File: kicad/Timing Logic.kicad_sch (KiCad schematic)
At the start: 38 parts, among them Q2 BC108, Q3 BC108, Q4 BD139, Q5 BC108, Q6 BC108, SW6 SW_SPDT, U6 4043, U7 4017, U8 HEF4093B, U9 TL431LP

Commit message: Starting docs
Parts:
- D14: footprint Diode_THT:D_DO-41_SOD81_P12.70mm_Horizontal -> Diode_THT:D_DO-35_SOD27_P7.62mm_Horizontal
- U9: footprint Package_TO_SOT_THT:TO-92 -> Package_TO_SOT_THT:TO-92_Inline
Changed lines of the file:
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@@
 (kicad_sch
-	(version 20231120)
+	(version 20250114)
 	(generator "eeschema")
-	(generator_version "8.0")
+	(generator_version "9.0")
 	(paper "A3")
 	(title_block
 		(title "PROM Programmer")
-		(date "2024-11-17")
-		(rev "V1.1")
+		(date "2025-03-27")
+		(rev "V1.4")
+	)
+	(text "Program\n(Push Button)\n"
+		(exclude_from_sim no)
+		(at 201.93 120.396 0)
+		(effects
+			(font
+				(size 1.27 1.27)
+			)
+		)
+	)
+	(text "Program"
+		(exclude_from_sim no)
+		(at 291.084 183.388 0)
+		(effects
+			(font
+				(size 1.27 1.27)
+			)
+		)
+	)
+	(text "Constant Current Source (65mA)\n"
+		(exclude_from_sim no)
+		(at 215.138 35.56 0)
+		(effects
+			(font
+				(size 1.27 1.27)
+			)
+		)
+	)
+	(text "Resistor = 2.5 / Io \nR = 16/0.065 = 38 \n\nIo = 2.5/47 = 53mA\n\nR = 1/(1/47 + 1/220) = 38.2\n"
+		(exclude_from_sim no)
+		(at 255.778 56.896 0)
+		(effects
+			(font
+				(size 1.27 1.27)
+			)
+		)
+	)
+	(text "Optional R to give \nvery close value\n"
+		(exclude_from_sim no)
+		(at 246.38 68.58 0)
+		(effects
+			(font
+				(size 0.635 0.635)
+			)
+		)
+	)
+	(text "0 = 10V Ouput\n1 = 0V output (BD139 shut down)"
+		(exclude_from_sim no)
+		(at 335.534 151.13 0)
+		(effects
+			(font
+				(size 1.27 1.27)
+			)
+			(justify left)
+		)
 	)
 	(junction
@@
 		)
 	)
-	(text "Program\n(Push Button)\n"
-		(exclude_from_sim no)
-		(at 201.93 120.396 0)
-		(effects
-			(font
-				(size 1.27 1.27)
-			)
-		)
-	)
-	(text "Program"
-		(exclude_from_sim no)
-		(at 291.084 183.388 0)
-		(effects
-			(font
-				(size 1.27 1.27)
-			)
-		)
-	)
-	(text "Constant Current Source (65mA)\n"
-		(exclude_from_sim no)
-		(at 215.138 35.56 0)
-		(effects
-			(font
-				(size 1.27 1.27)
-			)
-		)
-	)
-	(text "Resistor = 2.5 / Io \nR = 16/0.065 = 38 \n\nIo = 2.5/47 = 53mA\n\nR = 1/(1/47 + 1/220) = 38.2\n"
-		(exclude_from_sim no)
-		(at 255.778 56.896 0)
-		(effects
-			(font
-				(size 1.27 1.27)
-			)
-		)
-	)
-	(text "Optional R to give \nvery close value\n"
-		(exclude_from_sim no)
-		(at 246.38 68.58 0)
-		(effects
-			(font
-				(size 0.635 0.635)
-			)
-		)
-	)
-	(text "0 = 10V Ouput\n1 = 0V output (BD139 shut down)"
-		(exclude_from_sim no)
-		(at 335.534 151.13 0)
-		(effects
-			(font
-				(size 1.27 1.27)
-			)
-			(justify left)
-		)
-	)
 	(global_label "START"
 		(shape output)
@@
 			)
 		)
-		(property "Footprint" "Package_TO_SOT_THT:TO-92"
+		(property "Footprint" "Package_TO_SOT_THT:TO-92_Inline"
 			(at 207.264 63.5 0)
 			(effects
@@
 			)
 		)
-		(property "Footprint" "Diode_THT:D_DO-41_SOD81_P12.70mm_Horizontal"
+		(property "Footprint" "Diode_THT:D_DO-35_SOD27_P7.62mm_Horizontal"
 			(at 330.2 143.51 0)
 			(effects

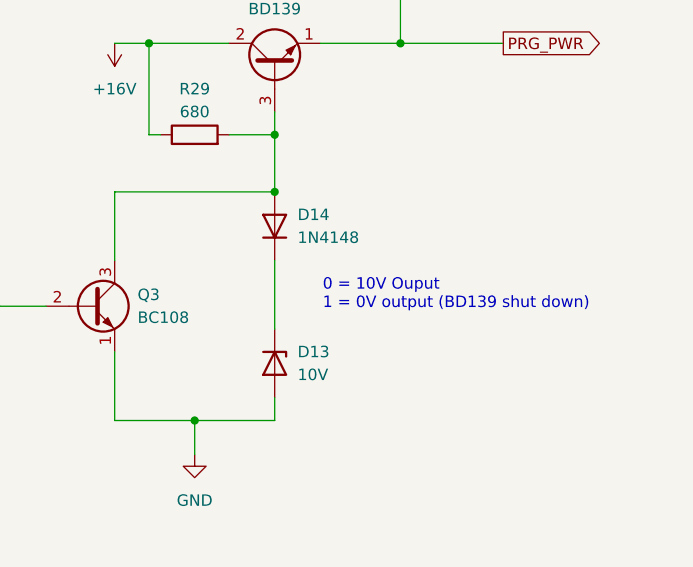
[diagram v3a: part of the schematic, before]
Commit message: Tweak layout, add part silkscreen values
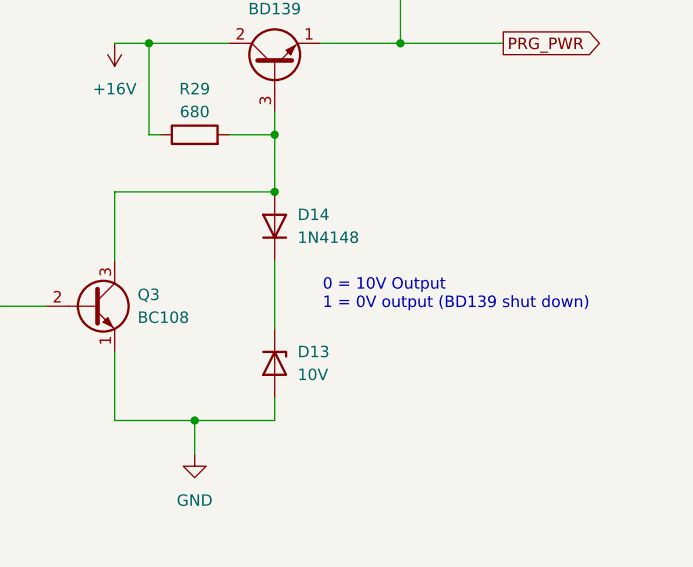
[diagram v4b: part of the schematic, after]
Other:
- note added: "0 = 10V Output 1 = 0V output (BD139 shut down)"
- note removed: "0 = 10V Ouput 1 = 0V output (BD139 shut down)"
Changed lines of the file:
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@@
 		)
 	)
-	(text "0 = 10V Ouput\n1 = 0V output (BD139 shut down)"
+	(text "0 = 10V Output\n1 = 0V output (BD139 shut down)"
 		(exclude_from_sim no)
 		(at 335.534 151.13 0)

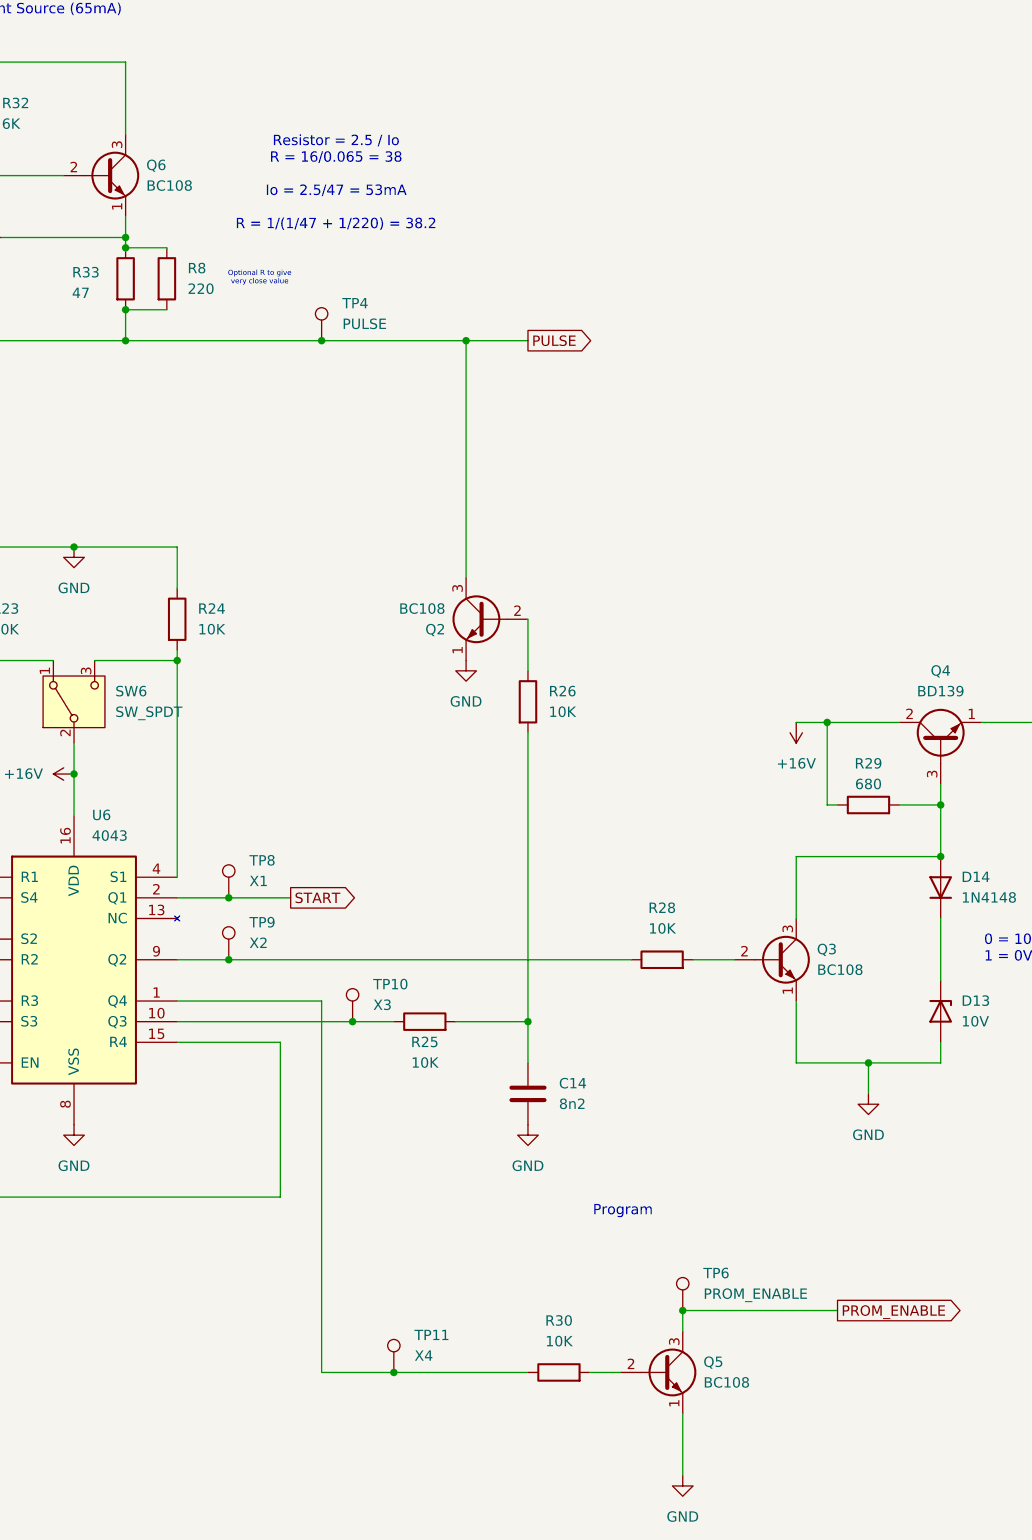
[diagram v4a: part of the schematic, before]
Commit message: Update transistors
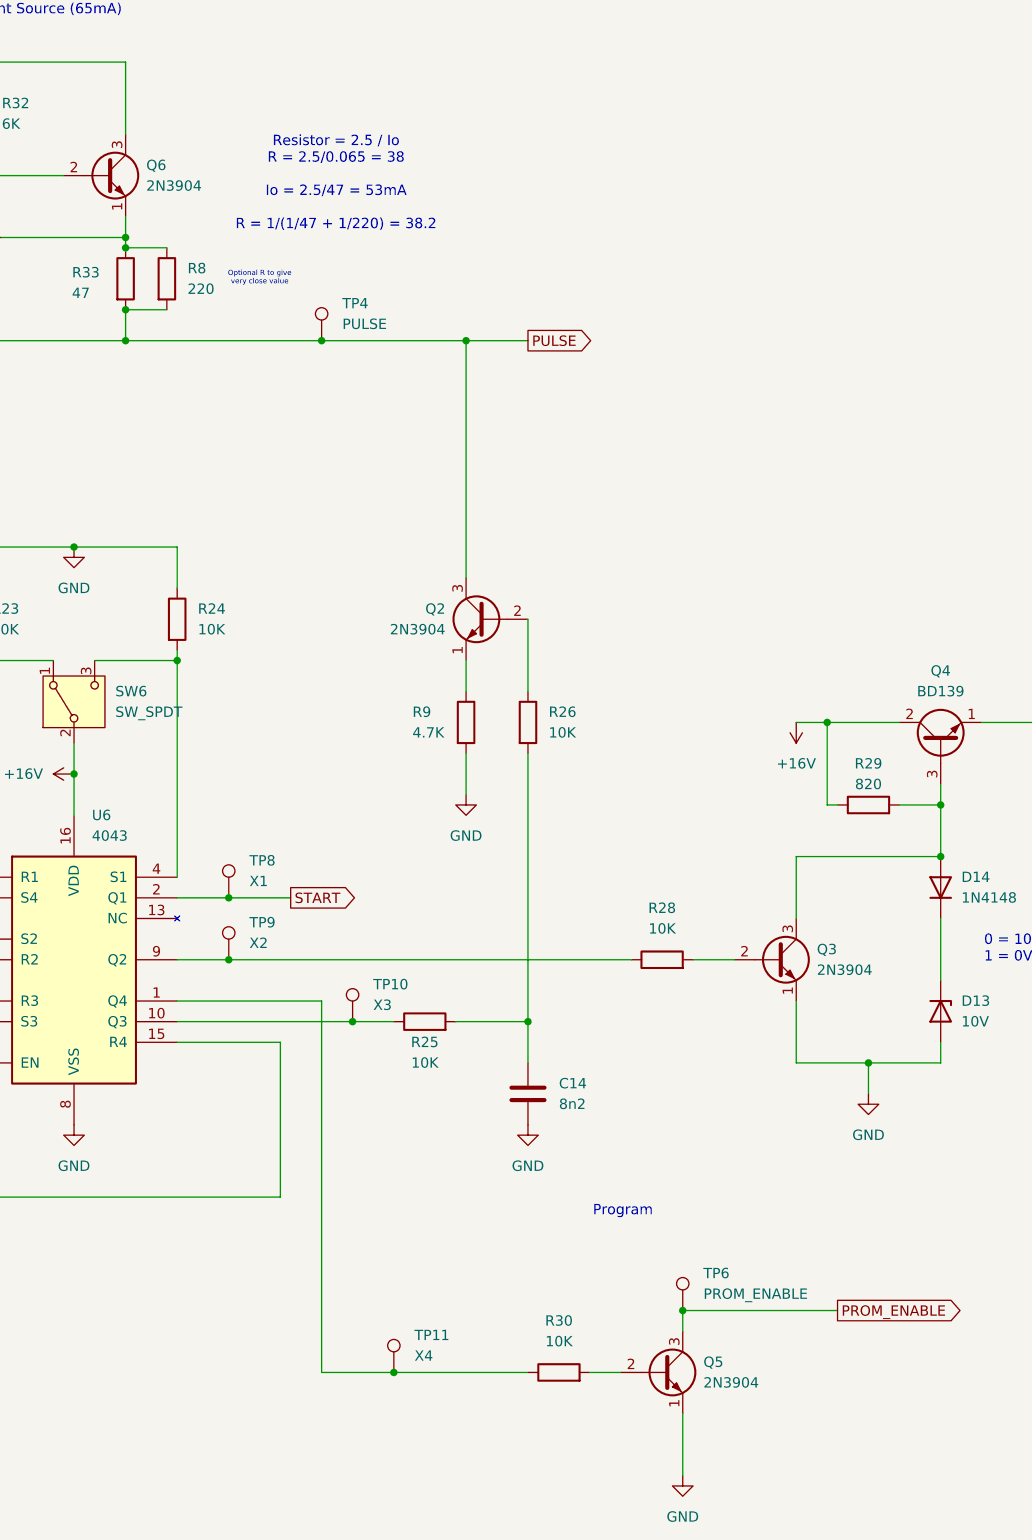
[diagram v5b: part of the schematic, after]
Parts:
- removed Q2, Q3, Q5, Q6: BC108, Package_TO_SOT_THT:TO-18-3, symbol Transistor_BJT:BC108
- added Q2, Q3, Q5, Q6: 2N3904, Package_TO_SOT_THT:TO-92_Inline, symbol Transistor_BJT:2N3904
- added R9: 4.7K, Resistor_THT:R_Axial_DIN0309_L9.0mm_D3.2mm_P12.70mm_Horizontal, symbol Device:R
- R29: value 680 -> 820
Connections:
- net +16V: now also Q6.3 (C)
- net GND: now also Q3.1 (E), Q5.1 (E), R9.2
- net PROM_ENABLE: now also Q5.3 (C)
- net PULSE: now also Q2.3 (C)
- net at R26.1: now also Q2.2 (B)
- net at R33.1, R8.1, U9.1 (REF): now also Q6.1 (E)
- net at R32.2, U9.3 (K): now also Q6.2 (B)
- net at R28.2: now also Q3.2 (B)
- net at D14.2 (A), Q4.3 (B), R29.2: now also Q3.3 (C)
- net at R30.2: now also Q5.2 (B)
- new net: Q2.1 (E), R9.1
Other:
- note added: "Resistor = 2.5 / Io R = 2.5/0.065 = 38 Io = 2.5/47 = 53mA R = 1/(1/47 + 1/220) = 38.2"
- note removed: "Resistor = 2.5 / Io R = 16/0.065 = 38 Io = 2.5/47 = 53mA R = 1/(1/47 + 1/220) = 38.2"
- moved on the sheet: R26
